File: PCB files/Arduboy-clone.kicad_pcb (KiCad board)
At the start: 2 copper layers, 65.1 x 106.8 mm, 35 parts, among them J1 USB_C_Receptacle_USB2.0_16P, J2 Conn_01x07, SW1 SW_Push, SW2 SW_Push, SW3 SW_Push, SW4 SW_Push, SW5 SW_Push, SW6 SW_Push, SW7 SW_Push, U1 ATmega32U4-A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

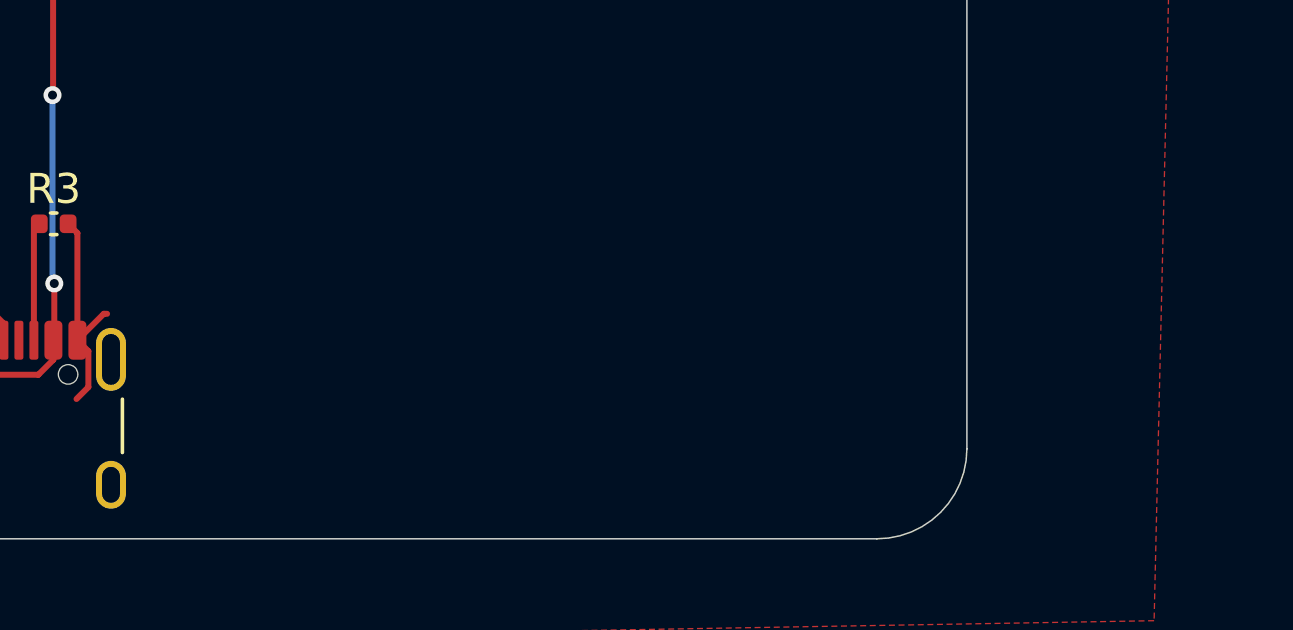
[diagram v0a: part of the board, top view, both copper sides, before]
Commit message: Added silkscreen customization
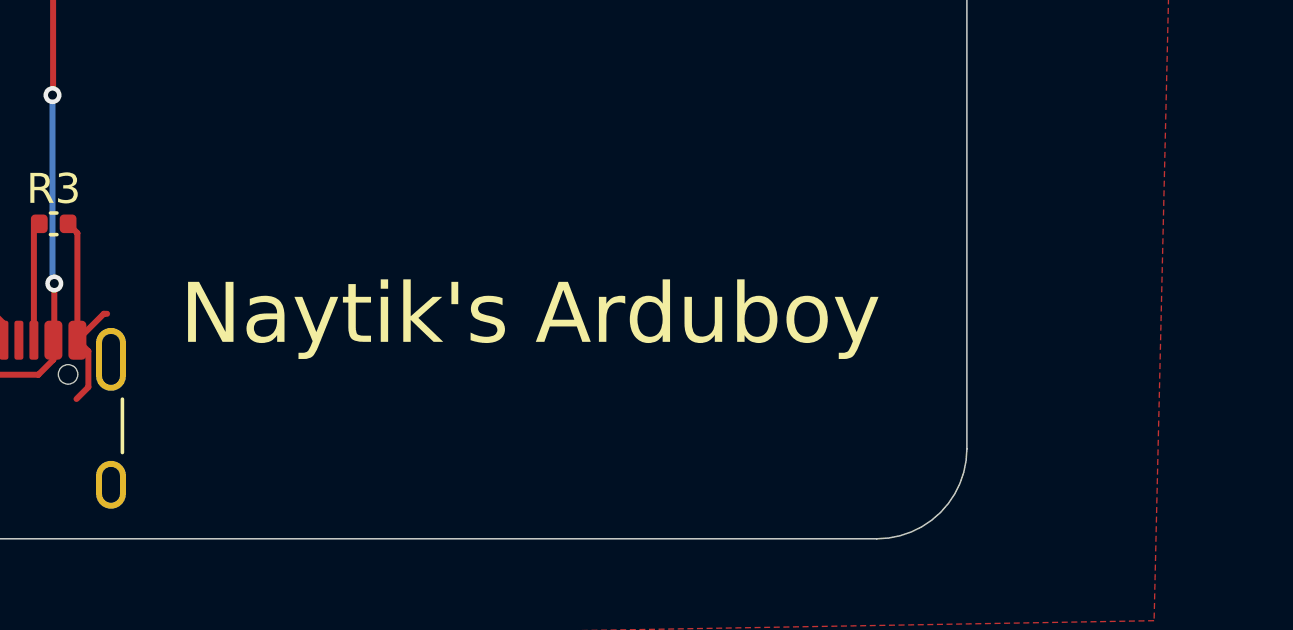
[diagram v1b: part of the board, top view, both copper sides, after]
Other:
- board text added: "Naytik's Arduboy"
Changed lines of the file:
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@@
 		(layer "Edge.Cuts")
+	)
+	(gr_text "Naytik's Arduboy"
+		(at 191.51 142.73 0)
+		(layer "F.SilkS")
+		(effects
+			(font
+				(size 2 2)
+				(thickness 0.25)
+			)
+			(justify left bottom)
+		)
 	)
 	(segment

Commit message: Added silkscreen art
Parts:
- added G***: LOGO, LOGO, B.Cu at (187.2, 95.5)
